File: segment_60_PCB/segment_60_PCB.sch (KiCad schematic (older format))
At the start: 127 parts, among them J1 BREAKOUT, SW1 SW_Push_45deg, SW10 SW_Push_45deg, SW11 SW_Push_45deg, SW12 SW_Push_45deg, SW13 SW_Push_45deg, SW14 SW_Push_45deg, SW15 SW_Push_45deg, SW16 SW_Push_45deg, SW17 SW_Push_45deg, SW18 SW_Push_45deg, SW19 SW_Push_45deg, SW2 SW_Push_45deg, SW20 SW_Push_45deg, SW21 SW_Push_45deg, SW22 SW_Push_45deg, SW23 SW_Push_45deg, SW24 SW_Push_45deg, SW25 SW_Push_45deg, SW26 SW_Push_45deg, SW27 SW_Push_45deg, SW28 SW_Push_45deg, SW29 SW_Push_45deg, SW3 SW_Push_45deg, SW30 SW_Push_45deg, SW31 SW_Push_45deg, SW32 SW_Push_45deg, SW33 SW_Push_45deg, SW34 SW_Push_45deg, SW35 SW_Push_45deg, SW36 SW_Push_45deg, SW37 SW_Push_45deg, SW38 SW_Push_45deg, SW39 SW_Push_45deg, SW4 SW_Push_45deg, SW40 SW_Push_45deg, SW41 SW_Push_45deg, SW42 SW_Push_45deg, SW43 SW_Push_45deg, SW44 SW_Push_45deg, SW45 SW_Push_45deg, SW46 SW_Push_45deg, SW47 SW_Push_45deg, SW48 SW_Push_45deg, SW49 SW_Push_45deg, SW5 SW_Push_45deg, SW50 SW_Push_45deg, SW51 SW_Push_45deg, SW52 SW_Push_45deg, SW53 SW_Push_45deg, SW54 SW_Push_45deg, SW55 SW_Push_45deg, SW56 SW_Push_45deg, SW57 SW_Push_45deg, SW58 SW_Push_45deg, SW59 SW_Push_45deg, SW6 SW_Push_45deg, SW60 SW_Push_45deg, SW61 SW_Push_45deg, SW62 SW_Push_45deg, SW63 SW_Push_45deg, SW64 SW_Push_45deg, SW65 SW_Push_45deg, SW66 SW_Push, SW67 SW_Push, SW7 SW_Push_45deg, SW8 SW_Push_45deg, SW9 SW_Push_45deg, U1 ATmega328P-PU, U10 74HC365, U11 74HC365, U12 74HC365, U13 74HC365, U14 74HC365, U15 74HC365, U16 74HC365, U17 74HC365, U2 74HC138, U3 74HC138, U4 74HC365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

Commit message: Updated symbols for 74HC365; routed all buffer to switch connections
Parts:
- U10, U11, U4, U5, U6, U7, U8, U9: symbol Segment_Symbols:74HC365 -> Segment_Symbols:74HC365_A
- U12, U14: symbol Segment_Symbols:74HC365 -> Segment_Symbols:74HC365_C
- U13, U15, U16: symbol Segment_Symbols:74HC365 -> Segment_Symbols:74HC365_B
- U17: symbol Segment_Symbols:74HC365 -> Segment_Symbols:74HC365_D
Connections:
- net at U12.11 (Y5): now also SW23.1; no longer SW9.1
- net at U12.13 (Y6): now also SW37.1; no longer SW23.1
- net at U12.3 (Y1): now also SW51.1; no longer SW37.1
- net at U12.5 (Y2): now also SW9.1; no longer SW51.1
- net at U13.11 (Y5): now also SW24.1; no longer SW10.1
- net at U13.13 (Y6): now also SW38.1; no longer SW24.1
- net at U13.3 (Y1): now also SW52.1; no longer SW38.1
- net at U13.5 (Y2): now also SW62.1; no longer SW52.1
- net at U13.7 (Y3): now also SW10.1; no longer SW62.1
- net at U14.11 (Y5): now also SW25.1; no longer SW11.1
- net at U14.13 (Y6): now also SW39.1; no longer SW25.1
- net at U14.3 (Y1): now also SW53.1; no longer SW39.1
- net at U14.5 (Y2): now also SW11.1; no longer SW53.1
- net at U15.11 (Y5): now also SW26.1; no longer SW12.1
- net at U15.13 (Y6): now also SW40.1; no longer SW26.1
- net at U15.3 (Y1): now also SW54.1; no longer SW40.1
- net at U15.5 (Y2): now also SW63.1; no longer SW54.1
- net at U15.7 (Y3): now also SW12.1; no longer SW63.1
- net at U16.11 (Y5): now also SW27.1; no longer SW13.1
- net at U16.13 (Y6): now also SW41.1; no longer SW27.1
- net at U16.3 (Y1): now also SW55.1; no longer SW41.1
- net at U16.5 (Y2): now also SW64.1; no longer SW55.1
- net at U16.7 (Y3): now also SW13.1; no longer SW64.1
- net at U17.11 (Y5): now also SW65.1; no longer SW14.1
- net at U17.13 (Y6): now also SW56.1; no longer SW28.1
- net at U17.5 (Y2): now also SW28.1; no longer SW56.1
- net at U17.7 (Y3): now also SW14.1; no longer SW65.1
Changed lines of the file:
@@
 	2100 7850 3000 7850
 $Comp
-L Segment_Symbols:74HC365 U4
+L Segment_Symbols:74HC365_A U4
 U 1 1 648384BE
 P 1450 1600
@@
 	1750 2200 1750 2000
 $Comp
-L Segment_Symbols:74HC365 U5
+L Segment_Symbols:74HC365_A U5
 U 1 1 64838502
 P 3100 1600
@@
 	1550 3650 3200 3650
 $Comp
-L Segment_Symbols:74HC365 U6
+L Segment_Symbols:74HC365_A U6
 U 1 1 6540ED25
 P 4750 1600
@@
 	5050 2200 5050 2000
 $Comp
-L Segment_Symbols:74HC365 U7
+L Segment_Symbols:74HC365_A U7
 U 1 1 6540ED69
 P 6400 1600
@@
 	4950 3350 6600 3350
 $Comp
-L Segment_Symbols:74HC365 U8
+L Segment_Symbols:74HC365_A U8
 U 1 1 65480DF8
 P 8050 1600
@@
 	8350 2200 8350 2000
 $Comp
-L Segment_Symbols:74HC365 U9
+L Segment_Symbols:74HC365_A U9
 U 1 1 65480E3C
 P 9700 1600
@@
 	8250 3350 9900 3350
 $Comp
-L Segment_Symbols:74HC365 U10
+L Segment_Symbols:74HC365_A U10
 U 1 1 6550EB54
 P 11350 1600
@@
 $EndComp
 $Comp
-L Segment_Symbols:74HC365 U11
+L Segment_Symbols:74HC365_A U11
 U 1 1 667D6AF3
 P 1450 4800
@@
 	1750 5400 1750 5200
 $Comp
-L Segment_Symbols:74HC365 U12
+L Segment_Symbols:74HC365_C U12
 U 1 1 667D6B31
 P 3100 4800
@@
 	1650 6550 3300 6550
 $Comp
-L Segment_Symbols:74HC365 U13
+L Segment_Symbols:74HC365_B U13
 U 1 1 667D6B92
 P 4750 4800
@@
 	5050 5400 5050 5200
 $Comp
-L Segment_Symbols:74HC365 U14
+L Segment_Symbols:74HC365_C U14
 U 1 1 667D6BD0
 P 6400 4800
@@
 	4950 6550 6600 6550
 $Comp
-L Segment_Symbols:74HC365 U15
+L Segment_Symbols:74HC365_B U15
 U 1 1 667D6C25
 P 8050 4800
@@
 	8350 5400 8350 5200
 $Comp
-L Segment_Symbols:74HC365 U16
+L Segment_Symbols:74HC365_B U16
 U 1 1 667D6C63
 P 9700 4800
@@
 	8150 6850 9800 6850
 $Comp
-L Segment_Symbols:74HC365 U17
+L Segment_Symbols:74HC365_D U17
 U 1 1 667D6CB8
 P 11350 4800
@@
 Wire Wire Line
 	6500 3600 6500 3650
+Connection ~ 6500 3650
+Wire Wire Line
+	6500 3650 9800 3650
 Wire Bus Line
 	15050 3550 15050 3950
@@
 Wire Bus Line
 	2850 8200 2850 9000
-Connection ~ 6500 3650
-Wire Wire Line
-	6500 3650 9800 3650
 $EndSCHEMATC

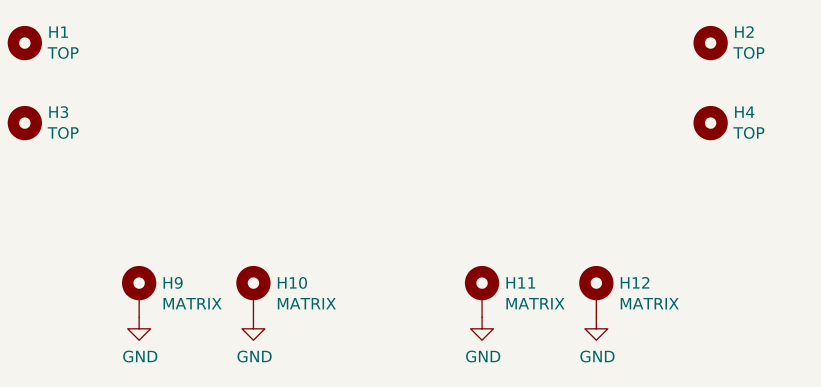
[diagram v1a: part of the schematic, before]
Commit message: Finished design and layout of SEGMENT-60 main PCB
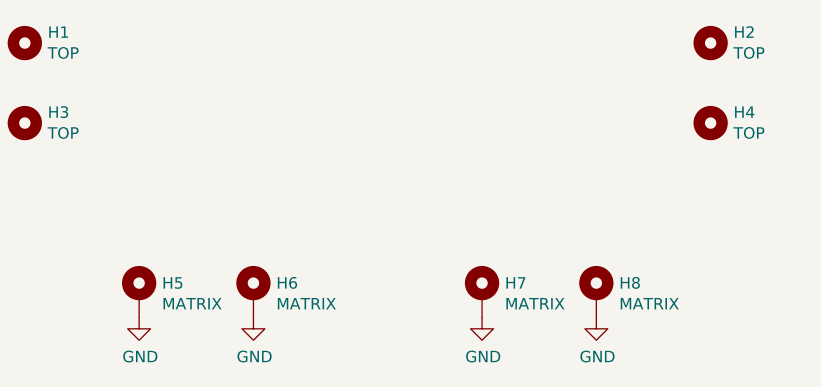
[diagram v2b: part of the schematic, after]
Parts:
- renumbered H9 to H5, H10 to H6, H11 to H7, H12 to H8
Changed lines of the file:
@@
 Entry Wire Line
 	2750 8100 2850 8200
-Text Label 5150 8600 0    50   ~ 0
-COL13
 Text Label 5150 8500 0    50   ~ 0
 COL12
@@
 SCL
 $Comp
-L Mechanical:MountingHole H1
-U 1 1 61F78669
-P 7500 9500
-F 0 "H1" H 7600 9546 50  0000 L CNN
-F 1 "TOP" H 7600 9455 50  0000 L CNN
-F 2 "MountingHole:MountingHole_3.2mm_M3" H 7500 9500 50  0001 C CNN
-F 3 "~" H 7500 9500 50  0001 C CNN
-	1    7500 9500
-	1    0    0    -1
-$EndComp
-$Comp
-L Mechanical:MountingHole H2
-U 1 1 61F7CD1E
-P 10500 9500
-F 0 "H2" H 10600 9546 50  0000 L CNN
-F 1 "TOP" H 10600 9455 50  0000 L CNN
-F 2 "MountingHole:MountingHole_3.2mm_M3" H 10500 9500 50  0001 C CNN
-F 3 "~" H 10500 9500 50  0001 C CNN
-	1    10500 9500
-	1    0    0    -1
-$EndComp
-$Comp
-L Mechanical:MountingHole H4
-U 1 1 61F7CF71
-P 10500 9850
-F 0 "H4" H 10600 9896 50  0000 L CNN
-F 1 "TOP" H 10600 9805 50  0000 L CNN
-F 2 "MountingHole:MountingHole_3.2mm_M3" H 10500 9850 50  0001 C CNN
-F 3 "~" H 10500 9850 50  0001 C CNN
-	1    10500 9850
-	1    0    0    -1
-$EndComp
-$Comp
-L Mechanical:MountingHole H3
-U 1 1 61F7D1CF
-P 7500 9850
-F 0 "H3" H 7600 9896 50  0000 L CNN
-F 1 "TOP" H 7600 9805 50  0000 L CNN
-F 2 "MountingHole:MountingHole_3.2mm_M3" H 7500 9850 50  0001 C CNN
-F 3 "~" H 7500 9850 50  0001 C CNN
-	1    7500 9850
-	1    0    0    -1
-$EndComp
-$Comp
-L Mechanical:MountingHole_Pad H9
+L Mechanical:MountingHole_Pad H5
 U 1 1 6203E4F6
 P 8000 10600
-F 0 "H9" H 8100 10649 50  0000 L CNN
+F 0 "H5" H 8100 10649 50  0000 L CNN
 F 1 "MATRIX" H 8100 10558 50  0000 L CNN
 F 2 "MountingHole:MountingHole_3.2mm_M3_Pad" H 8000 10600 50  0001 C CNN
@@
 $EndComp
 $Comp
-L power:GND #PWR013
-U 1 1 6203EB44
-P 8000 10700
-F 0 "#PWR013" H 8000 10450 50  0001 C CNN
-F 1 "GND" H 8005 10527 50  0000 C CNN
-F 2 "" H 8000 10700 50  0001 C CNN
-F 3 "" H 8000 10700 50  0001 C CNN
-	1    8000 10700
-	1    0    0    -1
-$EndComp
-$Comp
-L Mechanical:MountingHole_Pad H10
+L Mechanical:MountingHole_Pad H6
 U 1 1 620989EB
 P 8500 10600
-F 0 "H10" H 8600 10649 50  0000 L CNN
+F 0 "H6" H 8600 10649 50  0000 L CNN
 F 1 "MATRIX" H 8600 10558 50  0000 L CNN
 F 2 "MountingHole:MountingHole_3.2mm_M3_Pad" H 8500 10600 50  0001 C CNN
@@
 $EndComp
 $Comp
-L Mechanical:MountingHole_Pad H11
+L Mechanical:MountingHole_Pad H7
 U 1 1 620F22CB
 P 9500 10600
-F 0 "H11" H 9600 10649 50  0000 L CNN
+F 0 "H7" H 9600 10649 50  0000 L CNN
 F 1 "MATRIX" H 9600 10558 50  0000 L CNN
 F 2 "MountingHole:MountingHole_3.2mm_M3_Pad" H 9500 10600 50  0001 C CNN
@@
 $EndComp
 $Comp
-L Mechanical:MountingHole_Pad H12
+L Mechanical:MountingHole_Pad H8
 U 1 1 620F22E3
 P 10000 10600
-F 0 "H12" H 10100 10649 50  0000 L CNN
+F 0 "H8" H 10100 10649 50  0000 L CNN
 F 1 "MATRIX" H 10100 10558 50  0000 L CNN
 F 2 "MountingHole:MountingHole_3.2mm_M3_Pad" H 10000 10600 50  0001 C CNN
@@
 Wire Wire Line
 	6500 3650 9800 3650
+Text Label 5150 8600 0    50   ~ 0
+COL13
+Wire Bus Line
+	950  3950 10950 3950
+Wire Bus Line
+	950  750  10950 750
 Wire Bus Line
 	15050 3550 15050 3950
@@
 	1350 7900 1350 8500
 Wire Bus Line
-	5500 8200 5500 8800
-Wire Bus Line
-	950  750  10950 750
-Wire Bus Line
-	950  3950 10950 3950
-Wire Bus Line
 	2850 8200 2850 9000
+Wire Bus Line
+	5500 8200 5500 8800
+$Comp
+L power:GND #PWR013
+U 1 1 6203EB44
+P 8000 10700
+F 0 "#PWR013" H 8000 10450 50  0001 C CNN
+F 1 "GND" H 8005 10527 50  0000 C CNN
+F 2 "" H 8000 10700 50  0001 C CNN
+F 3 "" H 8000 10700 50  0001 C CNN
+	1    8000 10700
+	1    0    0    -1
+$EndComp
+$Comp
+L Mechanical:MountingHole H4
+U 1 1 61F7CF71
+P 10500 9850
+F 0 "H4" H 10600 9896 50  0000 L CNN
+F 1 "TOP" H 10600 9805 50  0000 L CNN
+F 2 "MountingHole:MountingHole_3.2mm_M3" H 10500 9850 50  0001 C CNN
+F 3 "~" H 10500 9850 50  0001 C CNN
+	1    10500 9850
+	1    0    0    -1
+$EndComp
+$Comp
+L Mechanical:MountingHole H2
+U 1 1 61F7CD1E
+P 10500 9500
+F 0 "H2" H 10600 9546 50  0000 L CNN
+F 1 "TOP" H 10600 9455 50  0000 L CNN
+F 2 "MountingHole:MountingHole_3.2mm_M3" H 10500 9500 50  0001 C CNN
+F 3 "~" H 10500 9500 50  0001 C CNN
+	1    10500 9500
+	1    0    0    -1
+$EndComp
+$Comp
+L Mechanical:MountingHole H3
+U 1 1 61F7D1CF
+P 7500 9850
+F 0 "H3" H 7600 9896 50  0000 L CNN
+F 1 "TOP" H 7600 9805 50  0000 L CNN
+F 2 "MountingHole:MountingHole_3.2mm_M3" H 7500 9850 50  0001 C CNN
+F 3 "~" H 7500 9850 50  0001 C CNN
+	1    7500 9850
+	1    0    0    -1
+$EndComp
+$Comp
+L Mechanical:MountingHole H1
+U 1 1 61F78669
+P 7500 9500
+F 0 "H1" H 7600 9546 50  0000 L CNN
+F 1 "TOP" H 7600 9455 50  0000 L CNN
+F 2 "MountingHole:MountingHole_3.2mm_M3" H 7500 9500 50  0001 C CNN
+F 3 "~" H 7500 9500 50  0001 C CNN
+	1    7500 9500
+	1    0    0    -1
+$EndComp
 $EndSCHEMATC
